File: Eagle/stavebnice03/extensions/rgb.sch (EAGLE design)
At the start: 6 parts

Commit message: fix of bugs on rgb and lipol board + a few minor changes
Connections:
- net N$6: now also U$8.6; no longer U$9.1
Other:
- moved on the sheet: R3
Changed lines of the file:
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@@
 <instance part="R1" gate="G$1" x="111.76" y="55.88" rot="R90"/>
 <instance part="R2" gate="G$1" x="121.92" y="55.88" rot="R90"/>
-<instance part="R3" gate="G$1" x="127" y="55.88" rot="R90"/>
+<instance part="R3" gate="G$1" x="187.96" y="55.88" rot="R90"/>
 </instances>
 <busses>
@@
 <segment>
 <wire x1="154.94" y1="86.36" x2="154.94" y2="91.44" width="0.1524" layer="91"/>
-<wire x1="154.94" y1="91.44" x2="127" y2="91.44" width="0.1524" layer="91"/>
+<wire x1="154.94" y1="91.44" x2="187.96" y2="91.44" width="0.1524" layer="91"/>
 <pinref part="U$1" gate="G$1" pin="1"/>
 <pinref part="R3" gate="G$1" pin="2"/>
-<wire x1="127" y1="60.96" x2="127" y2="91.44" width="0.1524" layer="91"/>
+<wire x1="187.96" y1="60.96" x2="187.96" y2="91.44" width="0.1524" layer="91"/>
 </segment>
 </net>
@@
 <segment>
 <pinref part="R3" gate="G$1" pin="1"/>
-<pinref part="U$9" gate="G$1" pin="1"/>
-<wire x1="127" y1="50.8" x2="127" y2="43.18" width="0.1524" layer="91"/>
+<pinref part="U$8" gate="G$1" pin="6"/>
+<wire x1="187.96" y1="50.8" x2="187.96" y2="43.18" width="0.1524" layer="91"/>
 </segment>
 </net>

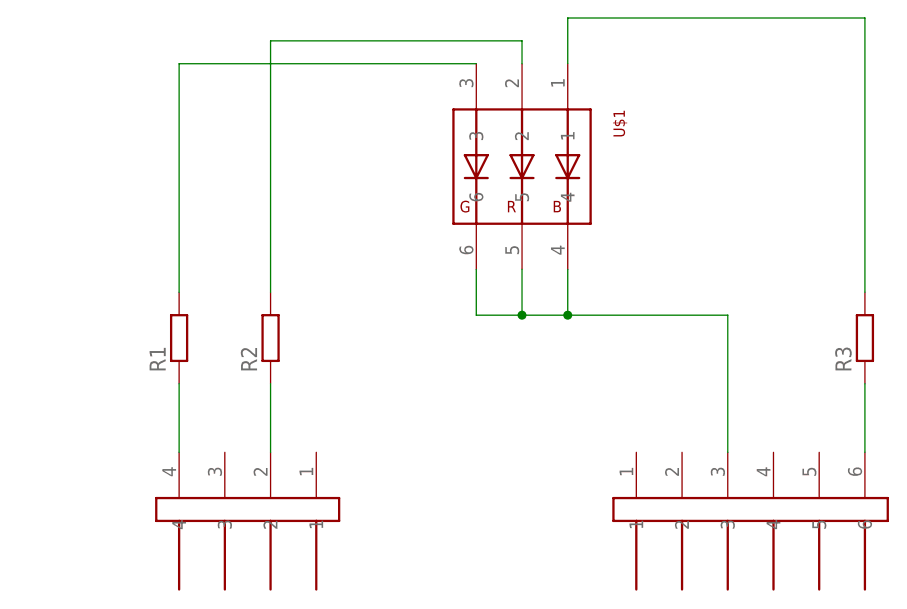
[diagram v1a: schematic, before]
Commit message: eagle adjustment for the Jíťa version
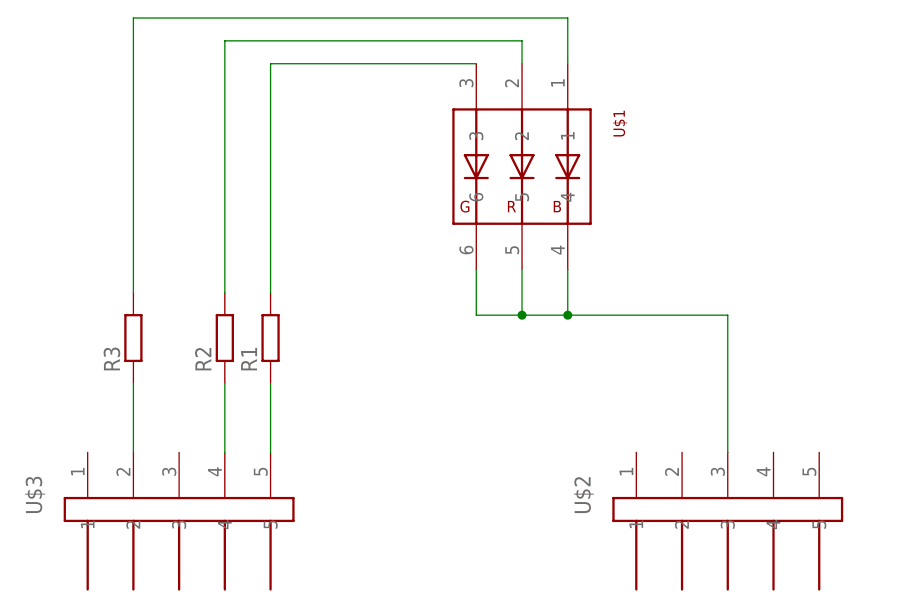
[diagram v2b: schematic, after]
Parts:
- removed U$8: JUMPER6M, !stavebnice03:JUMPER6M
- removed U$9: JUMPER4M, !stavebnice03:JUMPER4M
- added U$2, U$3: JUMPER5M, !stavebnice03:JUMPER5M
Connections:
- net GND: now also U$2.3; no longer U$8.3
- net N$1: now also R3.1, U$3.2; no longer R1.1, U$9.4
- net N$5: now also U$3.4; no longer U$9.2
- net N$6: now also R1.1, U$3.5; no longer R3.1, U$8.6
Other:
- moved on the sheet: R1, R2, R3
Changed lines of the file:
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@@
 </classes>
 <parts>
-<part name="U$8" library="!stavebnice03" deviceset="JUMPER6M" device=""/>
-<part name="U$9" library="!stavebnice03" deviceset="JUMPER4M" device=""/>
 <part name="U$1" library="!stavebnice03" deviceset="RGB_WW-FCE50TC-Q1" device=""/>
 <part name="R1" library="resistor" deviceset="R-EU_" device="R0603"/>
 <part name="R2" library="resistor" deviceset="R-EU_" device="R0603"/>
 <part name="R3" library="resistor" deviceset="R-EU_" device="R0603"/>
+<part name="U$2" library="!stavebnice03" deviceset="JUMPER5M" device=""/>
+<part name="U$3" library="!stavebnice03" deviceset="JUMPER5M" device=""/>
 </parts>
 <sheets>
@@
 </plain>
 <instances>
-<instance part="U$8" gate="G$1" x="175.26" y="35.56" rot="MR270"/>
-<instance part="U$9" gate="G$1" x="119.38" y="35.56" rot="R270"/>
 <instance part="U$1" gate="G$1" x="149.86" y="76.2" rot="R180"/>
-<instance part="R1" gate="G$1" x="111.76" y="55.88" rot="R90"/>
-<instance part="R2" gate="G$1" x="121.92" y="55.88" rot="R90"/>
-<instance part="R3" gate="G$1" x="187.96" y="55.88" rot="R90"/>
+<instance part="R1" gate="G$1" x="121.92" y="55.88" rot="R90"/>
+<instance part="R2" gate="G$1" x="116.84" y="55.88" rot="R90"/>
+<instance part="R3" gate="G$1" x="106.68" y="55.88" rot="R90"/>
+<instance part="U$2" gate="G$1" x="172.72" y="35.56" rot="MR270"/>
+<instance part="U$3" gate="G$1" x="111.76" y="35.56" rot="MR270"/>
 </instances>
 <busses>
@@
 <net name="GND" class="0">
 <segment>
-<pinref part="U$8" gate="G$1" pin="3"/>
 <wire x1="172.72" y1="43.18" x2="172.72" y2="58.42" width="0.1524" layer="91"/>
 <wire x1="172.72" y1="58.42" x2="154.94" y2="58.42" width="0.1524" layer="91"/>
@@
 <pinref part="U$1" gate="G$1" pin="5"/>
 <pinref part="U$1" gate="G$1" pin="6"/>
+<pinref part="U$2" gate="G$1" pin="3"/>
 </segment>
 </net>
 <net name="N$2" class="0">
 <segment>
-<wire x1="144.78" y1="86.36" x2="111.76" y2="86.36" width="0.1524" layer="91"/>
+<wire x1="144.78" y1="86.36" x2="121.92" y2="86.36" width="0.1524" layer="91"/>
 <pinref part="U$1" gate="G$1" pin="3"/>
 <pinref part="R1" gate="G$1" pin="2"/>
-<wire x1="111.76" y1="86.36" x2="111.76" y2="60.96" width="0.1524" layer="91"/>
+<wire x1="121.92" y1="86.36" x2="121.92" y2="60.96" width="0.1524" layer="91"/>
 </segment>
 </net>
@@
 <segment>
 <wire x1="149.86" y1="86.36" x2="149.86" y2="88.9" width="0.1524" layer="91"/>
-<wire x1="149.86" y1="88.9" x2="121.92" y2="88.9" width="0.1524" layer="91"/>
+<wire x1="149.86" y1="88.9" x2="116.84" y2="88.9" width="0.1524" layer="91"/>
 <pinref part="U$1" gate="G$1" pin="2"/>
 <pinref part="R2" gate="G$1" pin="2"/>
-<wire x1="121.92" y1="60.96" x2="121.92" y2="88.9" width="0.1524" layer="91"/>
+<wire x1="116.84" y1="60.96" x2="116.84" y2="88.9" width="0.1524" layer="91"/>
 </segment>
 </net>
@@
 <segment>
 <wire x1="154.94" y1="86.36" x2="154.94" y2="91.44" width="0.1524" layer="91"/>
-<wire x1="154.94" y1="91.44" x2="187.96" y2="91.44" width="0.1524" layer="91"/>
+<wire x1="154.94" y1="91.44" x2="106.68" y2="91.44" width="0.1524" layer="91"/>
 <pinref part="U$1" gate="G$1" pin="1"/>
 <pinref part="R3" gate="G$1" pin="2"/>
-<wire x1="187.96" y1="60.96" x2="187.96" y2="91.44" width="0.1524" layer="91"/>
+<wire x1="106.68" y1="60.96" x2="106.68" y2="91.44" width="0.1524" layer="91"/>
+</segment>
+</net>
+<net name="N$6" class="0">
+<segment>
+<pinref part="R1" gate="G$1" pin="1"/>
+<pinref part="U$3" gate="G$1" pin="5"/>
+<wire x1="121.92" y1="50.8" x2="121.92" y2="43.18" width="0.1524" layer="91"/>
 </segment>
 </net>
 <net name="N$1" class="0">
 <segment>
-<pinref part="R1" gate="G$1" pin="1"/>
-<pinref part="U$9" gate="G$1" pin="4"/>
-<wire x1="111.76" y1="50.8" x2="111.76" y2="43.18" width="0.1524" layer="91"/>
+<pinref part="R3" gate="G$1" pin="1"/>
+<pinref part="U$3" gate="G$1" pin="2"/>
+<wire x1="106.68" y1="50.8" x2="106.68" y2="43.18" width="0.1524" layer="91"/>
 </segment>
 </net>
@@
 <segment>
 <pinref part="R2" gate="G$1" pin="1"/>
-<pinref part="U$9" gate="G$1" pin="2"/>
-<wire x1="121.92" y1="50.8" x2="121.92" y2="43.18" width="0.1524" layer="91"/>
+<pinref part="U$3" gate="G$1" pin="4"/>
+<wire x1="116.84" y1="50.8" x2="116.84" y2="43.18" width="0.1524" layer="91"/>
 </segment>
 </net>
-<net name="N$6" class="0">
-<segment>
-<pinref part="R3" gate="G$1" pin="1"/>
-<pinref part="U$8" gate="G$1" pin="6"/>
-<wire x1="187.96" y1="50.8" x2="187.96" y2="43.18" width="0.1524" layer="91"/>
-</segment>
-</net>
